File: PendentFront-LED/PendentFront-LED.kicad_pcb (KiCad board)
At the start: 2 copper layers, 64 parts, among them J1 Conn_01x04_Pin, U1 74VHC9595FT, U2 74VHC9595FT, U3 74VHC9595FT

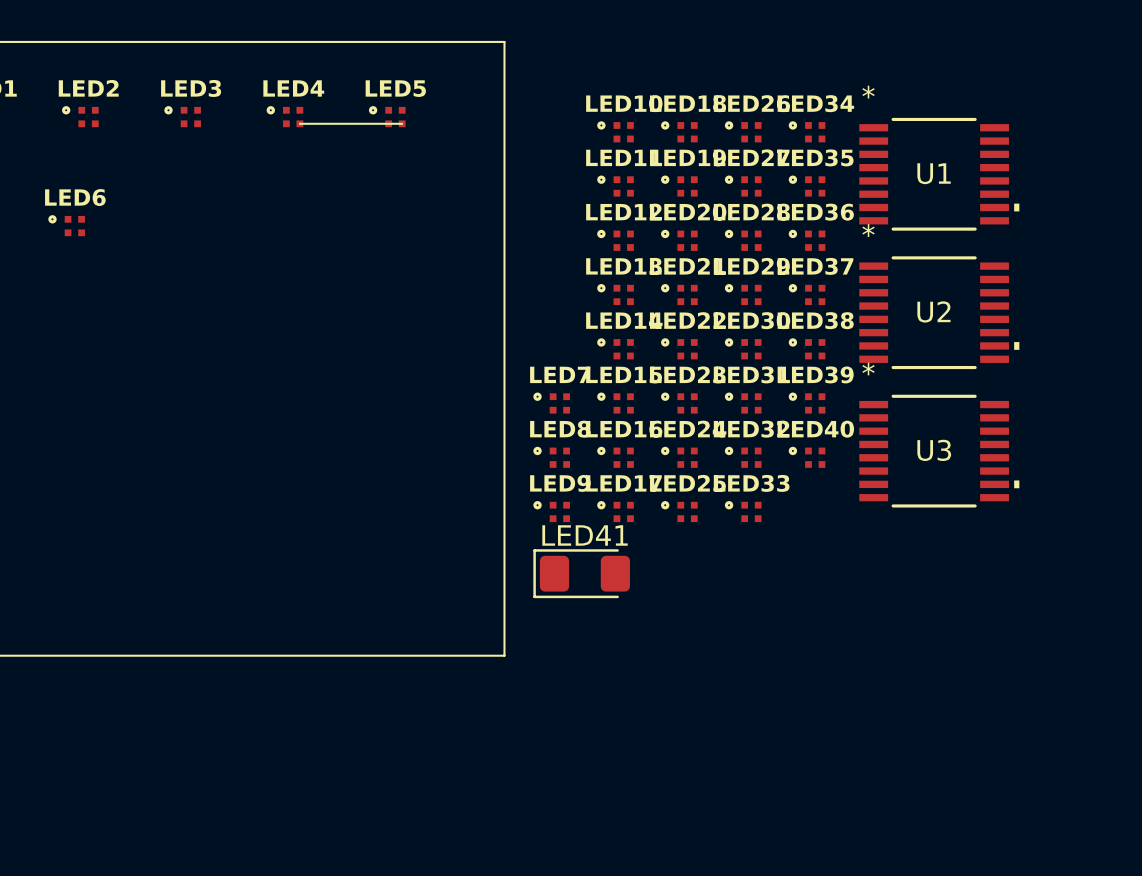
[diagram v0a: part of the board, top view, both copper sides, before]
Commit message: Added board outline to pcb
I need to manage my expectations
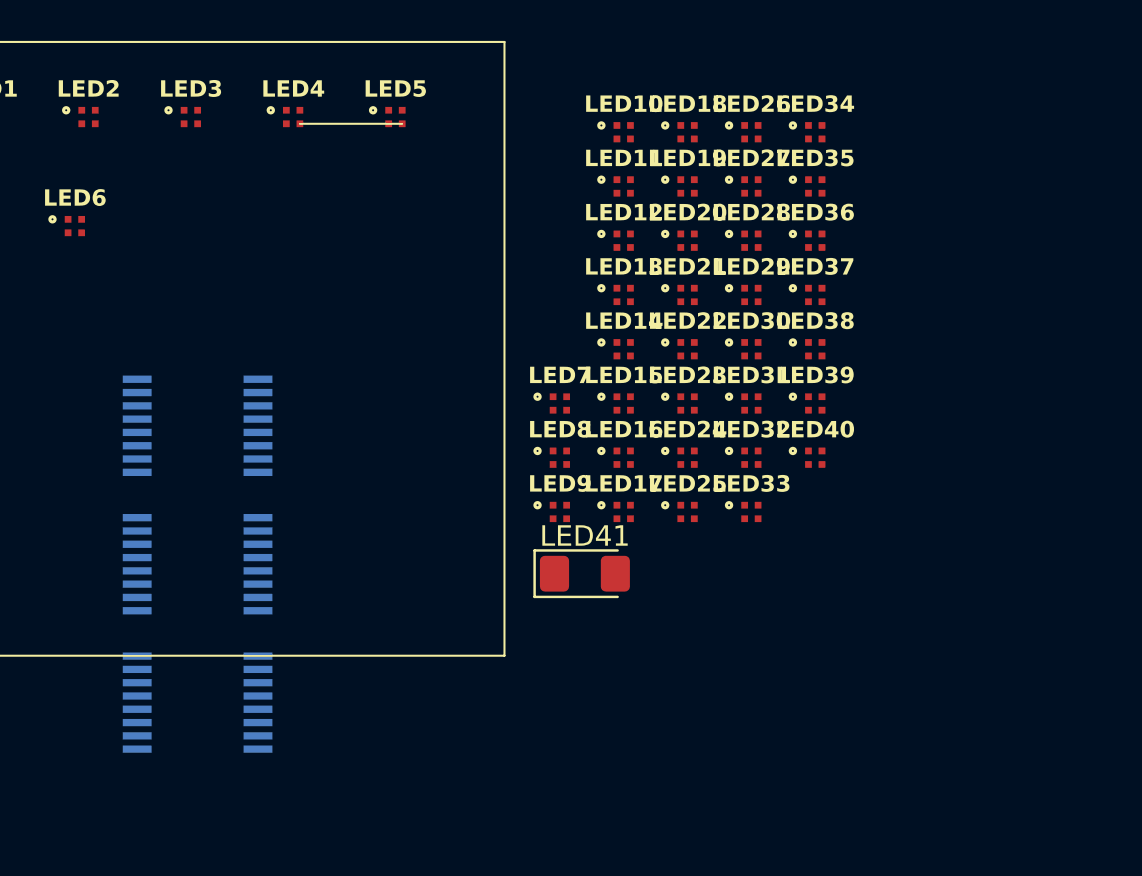
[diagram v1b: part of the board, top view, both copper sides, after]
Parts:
- U1, U2, U3: moved to B.Cu
- moved U1 44.3 mm to (65.0, 102.3)
- moved U2 38.0 mm to (65.0, 95.5)
- moved U3 36.0 mm to (65.0, 88.8)

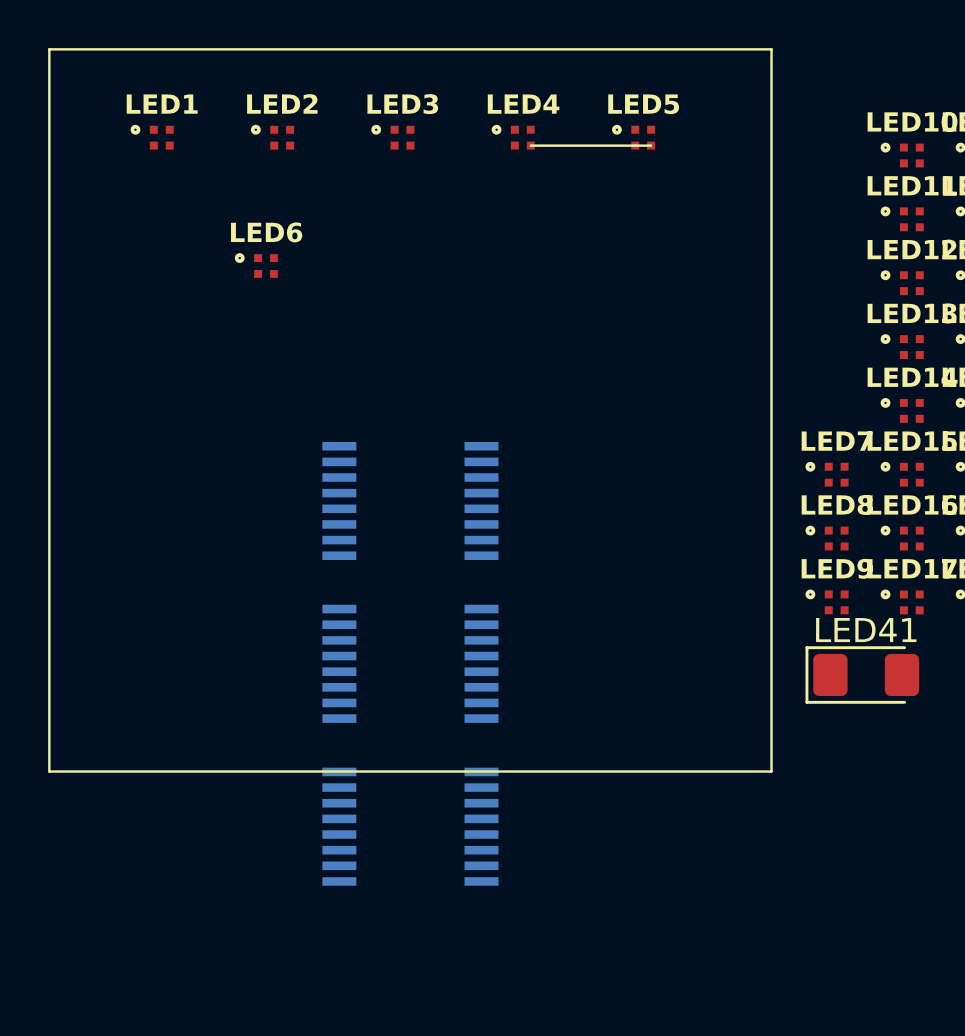
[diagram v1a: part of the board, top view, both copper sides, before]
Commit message: Added Shape Outlines
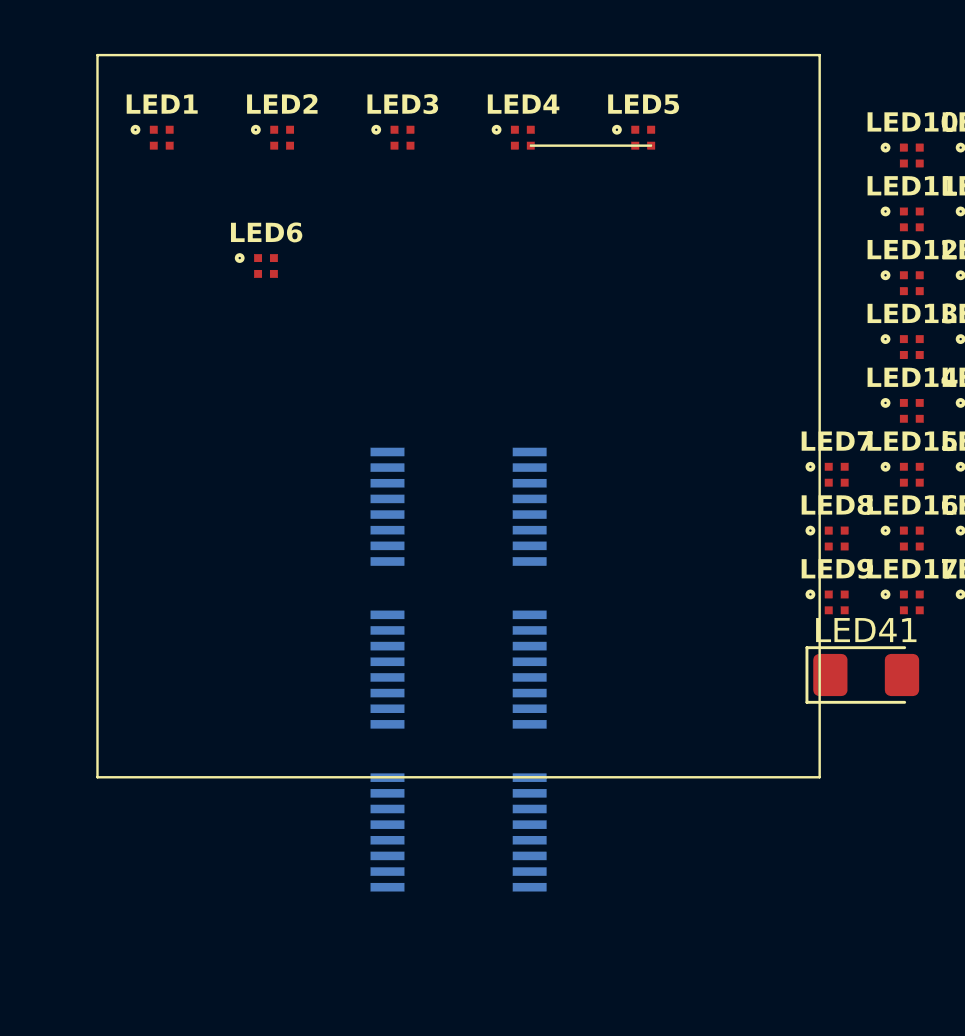
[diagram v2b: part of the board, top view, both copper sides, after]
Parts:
- moved U1 2.01 mm to (67.0, 102.5)
- moved U2 2.01 mm to (67.0, 95.8)
- moved U3 2.01 mm to (67.0, 89.0)
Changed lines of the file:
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@@
 	(footprint "PendentFrontFootprints:TSSOP16B_TOS"
 		(layer "B.Cu")
-		(at 65 95.526848)
+		(at 67 95.7658)
 		(tags "74VHC9595FT ")
 		(property "Reference" "U2"
@@
 	(footprint "PendentFrontFootprints:TSSOP16B_TOS"
 		(layer "B.Cu")
-		(at 65 102.292648)
+		(at 67 102.5316)
 		(tags "74VHC9595FT ")
 		(property "Reference" "U1"
@@
 	(footprint "PendentFrontFootprints:TSSOP16B_TOS"
 		(layer "B.Cu")
-		(at 65 88.761048)
+		(at 67 89)
 		(tags "74VHC9595FT ")
 		(property "Reference" "U3"
@@
 	)
 	(gr_rect
-		(start 50 70)
-		(end 80 100)
+		(start 52 70.238952)
+		(end 82 100.238952)
 		(stroke
 			(width 0.1)
@@
 	(gr_poly
 		(pts
-			(xy 65.254823 82.8551) (xy 65.661098 82.903371) (xy 66.061466 82.982863) (xy 66.455424 83.092791)
-			(xy 66.84247 83.232368) (xy 67.222101 83.40081) (xy 67.593814 83.597332) (xy 67.957107 83.821147)
-			(xy 68.311476 84.07147) (xy 68.656421 84.347517) (xy 68.991437 84.648502) (xy 69.316022 84.973638)
-			(xy 69.629673 85.322142) (xy 69.931888 85.693227) (xy 70.222165 86.086108) (xy 70.5 86.5) (xy 70.76489 86.934117)
-			(xy 71.016334 87.387674) (xy 71.253828 87.859885) (xy 71.476871 88.349966) (xy 71.684958 88.85713)
-			(xy 71.877588 89.380592) (xy 72.054258 89.919568) (xy 72.214465 90.47327) (xy 72.357707 91.040915)
-			(xy 72.48348 91.621717) (xy 72.591283 92.21489) (xy 72.680613 92.819649) (xy 72.750966 93.435208)
-			(xy 72.801841 94.060782) (xy 72.832734 94.695587) (xy 72.843144 95.338835) (xy 72.801841 96.616888)
-			(xy 72.680613 97.858021) (xy 72.48348 99.055953) (xy 72.214465 100.2044) (xy 71.877588 101.297078)
-			(xy 71.476871 102.327704) (xy 71.016334 103.289996) (xy 70.5 104.17767) (xy 69.931888 104.984443)
-			(xy 69.316022 105.704032) (xy 68.656421 106.330153) (xy 68.311476 106.6062) (xy 67.957107 106.856523)
-			(xy 67.593814 107.080338) (xy 67.222101 107.27686) (xy 66.84247 107.445302) (xy 66.455424 107.584879)
-			(xy 66.061466 107.694807) (xy 65.661098 107.774299) (xy 65.254823 107.82257) (xy 64.843144 107.838835)
-			(xy 64.431465 107.82257) (xy 64.02519 107.774299) (xy 63.624822 107.694807) (xy 63.230864 107.584879)
-			(xy 62.843818 107.445302) (xy 62.464187 107.27686) (xy 62.092474 107.080338) (xy 61.729182 106.856523)
-			(xy 61.374812 106.6062) (xy 61.029867 106.330153) (xy 60.694851 106.029168) (xy 60.370266 105.704032)
-			(xy 60.056615 105.355528) (xy 59.7544 104.984443) (xy 59.464123 104.591562) (xy 59.186288 104.17767)
-			(xy 58.921398 103.743553) (xy 58.669954 103.289996) (xy 58.43246 102.817785) (xy 58.209417 102.327704)
-			(xy 58.00133 101.82054) (xy 57.8087 101.297078) (xy 57.63203 100.758102) (xy 57.471823 100.2044)
-			(xy 57.328582 99.636755) (xy 57.202808 99.055953) (xy 57.095005 98.46278) (xy 57.005675 97.858021)
-			(xy 56.935322 97.242462) (xy 56.884447 96.616888) (xy 56.853554 95.982083) (xy 56.843144 95.338835)
-			(xy 56.884447 94.060782) (xy 57.005675 92.819649) (xy 57.202808 91.621717) (xy 57.471823 90.47327)
-			(xy 57.8087 89.380592) (xy 58.209417 88.349966) (xy 58.669954 87.387674) (xy 59.186288 86.5) (xy 59.7544 85.693227)
-			(xy 60.370266 84.973638) (xy 61.029867 84.347517) (xy 61.374812 84.07147) (xy 61.729182 83.821147)
-			(xy 62.092474 83.597332) (xy 62.464187 83.40081) (xy 62.843818 83.232368) (xy 63.230864 83.092791)
-			(xy 63.624822 82.982863) (xy 64.02519 82.903371) (xy 64.431465 82.8551) (xy 64.843144 82.838835)
+			(xy 39.842542 69.227131) (xy 40.295563 69.288612) (xy 40.741998 69.389856) (xy 41.181286 69.529864)
+			(xy 41.612866 69.707635) (xy 42.036179 69.92217) (xy 42.450662 70.172468) (xy 42.855756 70.457528)
+			(xy 43.250901 70.77635) (xy 43.635535 71.127934) (xy 44.009099 71.51128) (xy 44.371032 71.925387)
+			(xy 44.720773 72.369255) (xy 45.057762 72.841884) (xy 45.381438 73.342273) (xy 45.691241 73.869423)
+			(xy 45.986611 74.422331) (xy 46.266987 75) (xy 46.531808 75.601427) (xy 46.780514 76.225613) (xy 47.012545 76.871558)
+			(xy 47.227339 77.53826) (xy 47.424337 78.224721) (xy 47.602978 78.929939) (xy 47.762702 79.652914)
+			(xy 47.902947 80.392646) (xy 48.023154 81.148135) (xy 48.122763 81.91838) (xy 48.201211 82.702381)
+			(xy 48.25794 83.499137) (xy 48.292388 84.307649) (xy 48.303995 85.126916) (xy 48.25794 86.754694)
+			(xy 48.122763 88.335451) (xy 47.902947 89.861185) (xy 47.602978 91.323892) (xy 47.227339 92.715571)
+			(xy 46.780514 94.028219) (xy 46.266987 95.253832) (xy 45.691241 96.38441) (xy 45.057762 97.411948)
+			(xy 44.371032 98.328445) (xy 43.635535 99.125898) (xy 42.855756 99.796305) (xy 42.450662 100.081365)
+			(xy 42.036179 100.331663) (xy 41.612866 100.546198) (xy 41.181286 100.723969) (xy 40.741998 100.863977)
+			(xy 40.295563 100.965222) (xy 39.842542 101.026702) (xy 39.383494 101.047417) (xy 38.924446 101.026702)
+			(xy 38.471424 100.965222) (xy 38.024989 100.863977) (xy 37.585701 100.723969) (xy 37.154121 100.546198)
+			(xy 36.730809 100.331663) (xy 36.316325 100.081365) (xy 35.911231 99.796305) (xy 35.516087 99.477483)
+			(xy 35.131452 99.125898) (xy 34.757888 98.742552) (xy 34.395956 98.328445) (xy 34.046214 97.884577)
+			(xy 33.709226 97.411948) (xy 33.385549 96.911559) (xy 33.075746 96.38441) (xy 32.780376 95.831501)
+			(xy 32.5 95.253832) (xy 32.235179 94.652405) (xy 31.986473 94.028219) (xy 31.754443 93.382274) (xy 31.539648 92.715571)
+			(xy 31.34265 92.029111) (xy 31.164009 91.323892) (xy 31.004285 90.600917) (xy 30.86404 89.861185)
+			(xy 30.743833 89.105696) (xy 30.644225 88.335451) (xy 30.565776 87.551451) (xy 30.509047 86.754694)
+			(xy 30.474599 85.946182) (xy 30.462992 85.126916) (xy 30.509047 83.499137) (xy 30.644225 81.91838)
+			(xy 30.86404 80.392646) (xy 31.164009 78.929939) (xy 31.539648 77.53826) (xy 31.986473 76.225613)
+			(xy 32.5 75) (xy 33.075746 73.869423) (xy 33.709226 72.841884) (xy 34.395956 71.925387) (xy 35.131452 71.127934)
+			(xy 35.911231 70.457528) (xy 36.316325 70.172468) (xy 36.730809 69.92217) (xy 37.154121 69.707635)
+			(xy 37.585701 69.529864) (xy 38.024989 69.389856) (xy 38.471424 69.288612) (xy 38.924446 69.227131)
+			(xy 39.383494 69.206416)
 		)
 		(stroke
-			(width 0.133421)
+			(width 0.158999)
 			(type solid)
 		)
@@
 	)
 	(group ""
-		(members "04911132-6bf5-4ade-a816-51da1cac2345")
+		(members "7cc3657f-a1fd-4a7c-bc9f-16bca0e91c64")
 	)
 	(embedded_fonts no)

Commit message: Finalized pendent shape and started routing
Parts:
- removed LED1, LED10, LED11, LED12, LED13, LED14, LED15, LED16, LED17, LED18, LED19, LED2, LED20, LED21, LED22, LED23, LED24, LED25, LED26, LED27, LED28, LED29, LED3, LED30, LED31, LED32, LED33, LED34, LED35, LED36, LED37, LED38, LED39, LED4, LED40, LED5, LED6, LED7, LED8, LED9: UHD111A-FKA-C3K23E1L3VG5ZB3Z3, PendentFrontFootprints:SMD4_UHD111A-FKA_CRW
- removed LED41: AUX, LED_SMD:LED_1206_3216Metric_Pad1.42x1.75mm_HandSolder
- added D1: UHD111A-FKA-C3K23E1L3VG5ZB3Z3, PendentFrontFootprints:SMD4_UHD111A-FKA_CRW, F.Cu at (113.0, 52.0)
- added D10: UHD111A-FKA-C3K23E1L3VG5ZB3Z3, PendentFrontFootprints:SMD4_UHD111A-FKA_CRW, F.Cu at (113.0, 61.0)
- added D11: UHD111A-FKA-C3K23E1L3VG5ZB3Z3, PendentFrontFootprints:SMD4_UHD111A-FKA_CRW, F.Cu at (116.0, 61.0)
- added D12: UHD111A-FKA-C3K23E1L3VG5ZB3Z3, PendentFrontFootprints:SMD4_UHD111A-FKA_CRW, F.Cu at (119.0, 61.0)
- added D13: UHD111A-FKA-C3K23E1L3VG5ZB3Z3, PendentFrontFootprints:SMD4_UHD111A-FKA_CRW, F.Cu at (107.0, 64.0)
- added D14: UHD111A-FKA-C3K23E1L3VG5ZB3Z3, PendentFrontFootprints:SMD4_UHD111A-FKA_CRW, F.Cu at (110.0, 64.0)
- added D15: UHD111A-FKA-C3K23E1L3VG5ZB3Z3, PendentFrontFootprints:SMD4_UHD111A-FKA_CRW, F.Cu at (113.0, 64.0)
- added D16: UHD111A-FKA-C3K23E1L3VG5ZB3Z3, PendentFrontFootprints:SMD4_UHD111A-FKA_CRW, F.Cu at (116.0, 64.0)
- added D17: UHD111A-FKA-C3K23E1L3VG5ZB3Z3, PendentFrontFootprints:SMD4_UHD111A-FKA_CRW, F.Cu at (119.0, 64.0)
- added D18: UHD111A-FKA-C3K23E1L3VG5ZB3Z3, PendentFrontFootprints:SMD4_UHD111A-FKA_CRW, F.Cu at (122.0, 64.0)
- added D19: UHD111A-FKA-C3K23E1L3VG5ZB3Z3, PendentFrontFootprints:SMD4_UHD111A-FKA_CRW, F.Cu at (107.0, 67.0)
- added D2: UHD111A-FKA-C3K23E1L3VG5ZB3Z3, PendentFrontFootprints:SMD4_UHD111A-FKA_CRW, F.Cu at (116.0, 52.0)
- added D20: UHD111A-FKA-C3K23E1L3VG5ZB3Z3, PendentFrontFootprints:SMD4_UHD111A-FKA_CRW, F.Cu at (110.0, 67.0)
- added D21: UHD111A-FKA-C3K23E1L3VG5ZB3Z3, PendentFrontFootprints:SMD4_UHD111A-FKA_CRW, F.Cu at (113.0, 67.0)
- added D22: UHD111A-FKA-C3K23E1L3VG5ZB3Z3, PendentFrontFootprints:SMD4_UHD111A-FKA_CRW, F.Cu at (116.0, 67.0)
- added D23: UHD111A-FKA-C3K23E1L3VG5ZB3Z3, PendentFrontFootprints:SMD4_UHD111A-FKA_CRW, F.Cu at (119.0, 67.0)
- added D24: UHD111A-FKA-C3K23E1L3VG5ZB3Z3, PendentFrontFootprints:SMD4_UHD111A-FKA_CRW, F.Cu at (122.0, 67.0)
- added D25: UHD111A-FKA-C3K23E1L3VG5ZB3Z3, PendentFrontFootprints:SMD4_UHD111A-FKA_CRW, F.Cu at (104.0, 70.0)
- added D26: UHD111A-FKA-C3K23E1L3VG5ZB3Z3, PendentFrontFootprints:SMD4_UHD111A-FKA_CRW, F.Cu at (107.0, 70.0)
- added D27: UHD111A-FKA-C3K23E1L3VG5ZB3Z3, PendentFrontFootprints:SMD4_UHD111A-FKA_CRW, F.Cu at (110.0, 70.0)
- added D28: UHD111A-FKA-C3K23E1L3VG5ZB3Z3, PendentFrontFootprints:SMD4_UHD111A-FKA_CRW, F.Cu at (113.0, 70.0)
- added D29: UHD111A-FKA-C3K23E1L3VG5ZB3Z3, PendentFrontFootprints:SMD4_UHD111A-FKA_CRW, F.Cu at (116.0, 70.0)
- added D3: UHD111A-FKA-C3K23E1L3VG5ZB3Z3, PendentFrontFootprints:SMD4_UHD111A-FKA_CRW, F.Cu at (113.0, 55.0)
- added D30: UHD111A-FKA-C3K23E1L3VG5ZB3Z3, PendentFrontFootprints:SMD4_UHD111A-FKA_CRW, F.Cu at (119.0, 70.0)
- added D31: UHD111A-FKA-C3K23E1L3VG5ZB3Z3, PendentFrontFootprints:SMD4_UHD111A-FKA_CRW, F.Cu at (122.0, 70.0)
- added D32: UHD111A-FKA-C3K23E1L3VG5ZB3Z3, PendentFrontFootprints:SMD4_UHD111A-FKA_CRW, F.Cu at (125.0, 70.0)
- added D33: UHD111A-FKA-C3K23E1L3VG5ZB3Z3, PendentFrontFootprints:SMD4_UHD111A-FKA_CRW, F.Cu at (104.0, 73.0)
- added D34: UHD111A-FKA-C3K23E1L3VG5ZB3Z3, PendentFrontFootprints:SMD4_UHD111A-FKA_CRW, F.Cu at (107.0, 73.0)
- added D35: UHD111A-FKA-C3K23E1L3VG5ZB3Z3, PendentFrontFootprints:SMD4_UHD111A-FKA_CRW, F.Cu at (110.0, 73.0)
- added D36: UHD111A-FKA-C3K23E1L3VG5ZB3Z3, PendentFrontFootprints:SMD4_UHD111A-FKA_CRW, F.Cu at (113.0, 73.0)
- added D37: UHD111A-FKA-C3K23E1L3VG5ZB3Z3, PendentFrontFootprints:SMD4_UHD111A-FKA_CRW, F.Cu at (116.0, 73.0)
- added D38: UHD111A-FKA-C3K23E1L3VG5ZB3Z3, PendentFrontFootprints:SMD4_UHD111A-FKA_CRW, F.Cu at (119.0, 73.0)
- added D39: UHD111A-FKA-C3K23E1L3VG5ZB3Z3, PendentFrontFootprints:SMD4_UHD111A-FKA_CRW, F.Cu at (122.0, 73.0)
- added D4: UHD111A-FKA-C3K23E1L3VG5ZB3Z3, PendentFrontFootprints:SMD4_UHD111A-FKA_CRW, F.Cu at (116.0, 55.0)
- added D40: UHD111A-FKA-C3K23E1L3VG5ZB3Z3, PendentFrontFootprints:SMD4_UHD111A-FKA_CRW, F.Cu at (125.0, 73.0)
- added D41: UHD111A-FKA-C3K23E1L3VG5ZB3Z3, PendentFrontFootprints:SMD4_UHD111A-FKA_CRW, F.Cu at (104.0, 76.0)
- added D42: UHD111A-FKA-C3K23E1L3VG5ZB3Z3, PendentFrontFootprints:SMD4_UHD111A-FKA_CRW, F.Cu at (107.0, 76.0)
- added D43: UHD111A-FKA-C3K23E1L3VG5ZB3Z3, PendentFrontFootprints:SMD4_UHD111A-FKA_CRW, F.Cu at (110.0, 76.0)
- added D44: UHD111A-FKA-C3K23E1L3VG5ZB3Z3, PendentFrontFootprints:SMD4_UHD111A-FKA_CRW, F.Cu at (113.0, 76.0)
- added D45: UHD111A-FKA-C3K23E1L3VG5ZB3Z3, PendentFrontFootprints:SMD4_UHD111A-FKA_CRW, F.Cu at (116.0, 76.0)
- added D46: UHD111A-FKA-C3K23E1L3VG5ZB3Z3, PendentFrontFootprints:SMD4_UHD111A-FKA_CRW, F.Cu at (119.0, 76.0)
- added D47: UHD111A-FKA-C3K23E1L3VG5ZB3Z3, PendentFrontFootprints:SMD4_UHD111A-FKA_CRW, F.Cu at (122.0, 76.0)
- added D48: UHD111A-FKA-C3K23E1L3VG5ZB3Z3, PendentFrontFootprints:SMD4_UHD111A-FKA_CRW, F.Cu at (125.0, 76.0)
- added D49: UHD111A-FKA-C3K23E1L3VG5ZB3Z3, PendentFrontFootprints:SMD4_UHD111A-FKA_CRW, F.Cu at (104.0, 79.0)
- added D5: UHD111A-FKA-C3K23E1L3VG5ZB3Z3, PendentFrontFootprints:SMD4_UHD111A-FKA_CRW, F.Cu at (110.0, 58.0)
- added D50: UHD111A-FKA-C3K23E1L3VG5ZB3Z3, PendentFrontFootprints:SMD4_UHD111A-FKA_CRW, F.Cu at (107.0, 79.0)
- added D51: UHD111A-FKA-C3K23E1L3VG5ZB3Z3, PendentFrontFootprints:SMD4_UHD111A-FKA_CRW, F.Cu at (110.0, 79.0)
- added D52: UHD111A-FKA-C3K23E1L3VG5ZB3Z3, PendentFrontFootprints:SMD4_UHD111A-FKA_CRW, F.Cu at (113.0, 79.0)
- added D53: UHD111A-FKA-C3K23E1L3VG5ZB3Z3, PendentFrontFootprints:SMD4_UHD111A-FKA_CRW, F.Cu at (116.0, 79.0)
- added D54: UHD111A-FKA-C3K23E1L3VG5ZB3Z3, PendentFrontFootprints:SMD4_UHD111A-FKA_CRW, F.Cu at (119.0, 79.0)
- added D55: UHD111A-FKA-C3K23E1L3VG5ZB3Z3, PendentFrontFootprints:SMD4_UHD111A-FKA_CRW, F.Cu at (122.0, 79.0)
- added D56: UHD111A-FKA-C3K23E1L3VG5ZB3Z3, PendentFrontFootprints:SMD4_UHD111A-FKA_CRW, F.Cu at (125.0, 79.0)
- added D57: UHD111A-FKA-C3K23E1L3VG5ZB3Z3, PendentFrontFootprints:SMD4_UHD111A-FKA_CRW, F.Cu at (107.0, 82.0)
- added D58: UHD111A-FKA-C3K23E1L3VG5ZB3Z3, PendentFrontFootprints:SMD4_UHD111A-FKA_CRW, F.Cu at (110.0, 82.0)
- added D59: UHD111A-FKA-C3K23E1L3VG5ZB3Z3, PendentFrontFootprints:SMD4_UHD111A-FKA_CRW, F.Cu at (113.0, 82.0)
- added D6: UHD111A-FKA-C3K23E1L3VG5ZB3Z3, PendentFrontFootprints:SMD4_UHD111A-FKA_CRW, F.Cu at (113.0, 58.0)
- added D60: UHD111A-FKA-C3K23E1L3VG5ZB3Z3, PendentFrontFootprints:SMD4_UHD111A-FKA_CRW, F.Cu at (116.0, 82.0)
- added D61: UHD111A-FKA-C3K23E1L3VG5ZB3Z3, PendentFrontFootprints:SMD4_UHD111A-FKA_CRW, F.Cu at (119.0, 82.0)
- added D62: UHD111A-FKA-C3K23E1L3VG5ZB3Z3, PendentFrontFootprints:SMD4_UHD111A-FKA_CRW, F.Cu at (122.0, 82.0)
- added D63: UHD111A-FKA-C3K23E1L3VG5ZB3Z3, PendentFrontFootprints:SMD4_UHD111A-FKA_CRW, F.Cu at (113.0, 85.0)
- added D64: UHD111A-FKA-C3K23E1L3VG5ZB3Z3, PendentFrontFootprints:SMD4_UHD111A-FKA_CRW, F.Cu at (116.0, 85.0)
- added D65: AUX, LED_SMD:LED_1206_3216Metric_Pad1.42x1.75mm_HandSolder, F.Cu at (78.4, 63.9)
- added D7: UHD111A-FKA-C3K23E1L3VG5ZB3Z3, PendentFrontFootprints:SMD4_UHD111A-FKA_CRW, F.Cu at (116.0, 58.0)
- added D8: UHD111A-FKA-C3K23E1L3VG5ZB3Z3, PendentFrontFootprints:SMD4_UHD111A-FKA_CRW, F.Cu at (119.0, 58.0)
- added D9: UHD111A-FKA-C3K23E1L3VG5ZB3Z3, PendentFrontFootprints:SMD4_UHD111A-FKA_CRW, F.Cu at (110.0, 61.0)
- added R17: R, Resistor_SMD:R_0402_1005Metric_Pad0.72x0.64mm_HandSolder, F.Cu at (96.0, 50.1)
- added R18: R, Resistor_SMD:R_0402_1005Metric_Pad0.72x0.64mm_HandSolder, F.Cu at (96.0, 52.1)
- added R19: R, Resistor_SMD:R_0402_1005Metric_Pad0.72x0.64mm_HandSolder, F.Cu at (96.0, 54.1)
- added R20: R, Resistor_SMD:R_0402_1005Metric_Pad0.72x0.64mm_HandSolder, F.Cu at (96.0, 56.1)
- added R21: R, Resistor_SMD:R_0402_1005Metric_Pad0.72x0.64mm_HandSolder, F.Cu at (96.0, 58.1)
- added R22: R, Resistor_SMD:R_0402_1005Metric_Pad0.72x0.64mm_HandSolder, F.Cu at (96.0, 60.1)
- added R23: R, Resistor_SMD:R_0402_1005Metric_Pad0.72x0.64mm_HandSolder, F.Cu at (96.0, 62.0)
- added R24: R, Resistor_SMD:R_0402_1005Metric_Pad0.72x0.64mm_HandSolder, F.Cu at (96.0, 64.0)
- added R25: R, Resistor_SMD:R_0402_1005Metric_Pad0.72x0.64mm_HandSolder, F.Cu at (96.0, 66.0)
- added U4: 74VHC9595FT, PendentFrontFootprints:TSSOP16B_TOS, B.Cu at (67.0, 82.5)
- J1: value Conn_01x04_Pin -> Conn_01x05_Pin; footprint Connector_PinHeader_2.54mm:PinHeader_1x04_P2.54mm_Vertical -> Connector_PinHeader_1.27mm:PinHeader_1x05_P1.27mm_Vertical
- moved U1 76.2 mm to (124.6, 52.6), turned to -90 degrees
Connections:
- J1 pad 3: SerialIn -> RCK
- J1 pad 4: GND -> SerialIn
- R16 pad 2: GND -> /COLOR.BLUE6
- U1 pad 10: /COL5 -> unconnected-(U1-Q5-Pad10)
- U1 pad 11: /COL6 -> unconnected-(U1-Q6-Pad11)
- U1 pad 12: /COL7 -> unconnected-(U1-Q7-Pad12)
- U1 pad 13: /COL8 -> unconnected-(U1-Q8-Pad13)
- U1 pad 5: /COL1 -> unconnected-(U1-Q1-Pad5)
- U1 pad 6: /COL2 -> unconnected-(U1-Q2-Pad6)
- U1 pad 7: /COL3 -> unconnected-(U1-Q3-Pad7)
- U1 pad 9: /COL4 -> unconnected-(U1-Q4-Pad9)
- U2 pad 10: /COLOR.RED5 -> unconnected-(U2-Q5-Pad10)
- U2 pad 11: /COLOR.GREEN1 -> unconnected-(U2-Q6-Pad11)
- U2 pad 12: /COLOR.GREEN2 -> unconnected-(U2-Q7-Pad12)
- U2 pad 13: /COLOR.GREEN3 -> unconnected-(U2-Q8-Pad13)
- U2 pad 5: /COLOR.RED1 -> unconnected-(U2-Q1-Pad5)
- U2 pad 6: /COLOR.RED2 -> unconnected-(U2-Q2-Pad6)
- U2 pad 7: /COLOR.RED3 -> unconnected-(U2-Q3-Pad7)
- U2 pad 9: /COLOR.RED4 -> unconnected-(U2-Q4-Pad9)
- U3 pad 10: /COLOR.BLUE3 -> unconnected-(U3-Q5-Pad10)
- U3 pad 11: /COLOR.BLUE4 -> unconnected-(U3-Q6-Pad11)
- U3 pad 12: /COLOR.BLUE5 -> unconnected-(U3-Q7-Pad12)
- U3 pad 13: /AUX_LED -> unconnected-(U3-Q8-Pad13)
- U3 pad 15: unconnected-(U3-Q8C-Pad15) -> Net-(U3-Q8C)
- U3 pad 5: /COLOR.GREEN4 -> unconnected-(U3-Q1-Pad5)
- U3 pad 6: /COLOR.GREEN5 -> unconnected-(U3-Q2-Pad6)
- U3 pad 7: /COLOR.BLUE1 -> unconnected-(U3-Q3-Pad7)
- U3 pad 9: /COLOR.BLUE2 -> unconnected-(U3-Q4-Pad9)
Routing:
- net Net-(D57-Pad1): track 0.00 -> 37.5 mm, vias 0 -> 2
- net Net-(D49-Pad1): track 0.00 -> 30.6 mm
- net Net-(D41-Pad1): track 0.00 -> 30.6 mm
- net Net-(D33-Pad1): track 0.00 -> 30.6 mm
- net Net-(D25-Pad1): track 0.00 -> 29.5 mm
- net Net-(D1-Pad3): track 0.00 -> 27.8 mm, vias 0 -> 4
- net Net-(D17-Pad3): track 0.00 -> 27.6 mm
- net Net-(D17-Pad1): track 0.00 -> 27.0 mm, vias 0 -> 2
- net Net-(D10-Pad1): track 0.00 -> 26.7 mm, vias 0 -> 2
- net Net-(D10-Pad3): track 0.00 -> 26.7 mm, vias 0 -> 2
- net Net-(D57-Pad3): track 0.00 -> 26.6 mm, vias 0 -> 2
- net Net-(D49-Pad3): track 0.00 -> 25.9 mm
- net Net-(D41-Pad3): track 0.00 -> 25.9 mm
- net Net-(D33-Pad3): track 0.00 -> 25.9 mm
- net Net-(D25-Pad3): track 0.00 -> 25.9 mm
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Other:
- board outline added: 25.7 x 39.2 mm
